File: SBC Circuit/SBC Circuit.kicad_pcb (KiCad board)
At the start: 2 copper layers, 127 x 114.3 mm, 82 parts, among them J1 USB_B, J2 Conn_01x02_Pin, J3 Conn_01x06_Pin, J4 Conn_01x06_Pin, J5 Conn_01x03_Pin, J6 Conn_01x08_Pin, J7 Conn_01x06_Pin, J8 Conn_01x02_Pin, J9 Conn_02x04_Odd_Even, Q1 AOI21357, Q2 AOI21357, SW1 RESET, U1 MC68000FN, U10 FT230XS, U11 MC34064P, U2 XC9572XL, U3 68681, U4 MCM6206CP, U5 MCM6206CP, U6 28C256, U7 28C256, U8 LM7805_TO220, U9 LD1117AV33, X1 SG-531, X2 EC11

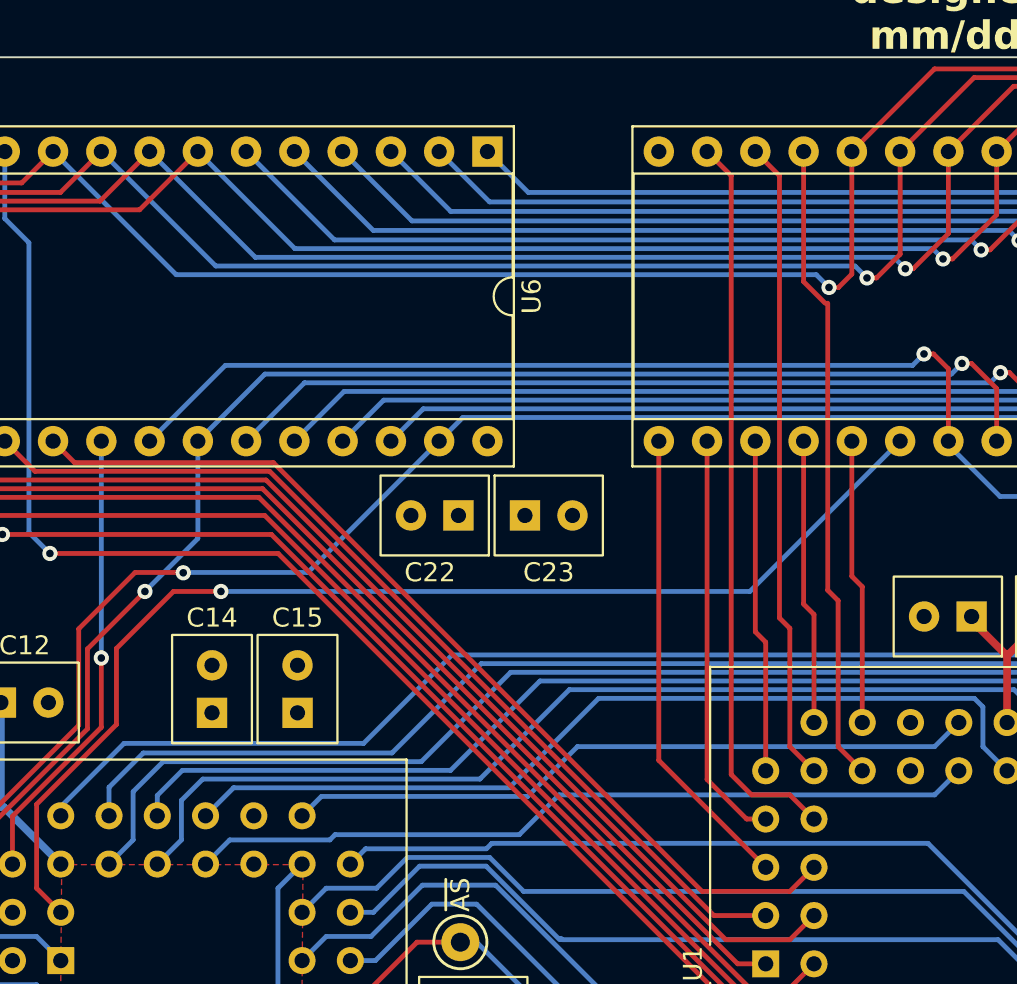
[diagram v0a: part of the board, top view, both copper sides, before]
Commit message: Wire high ROM correctly
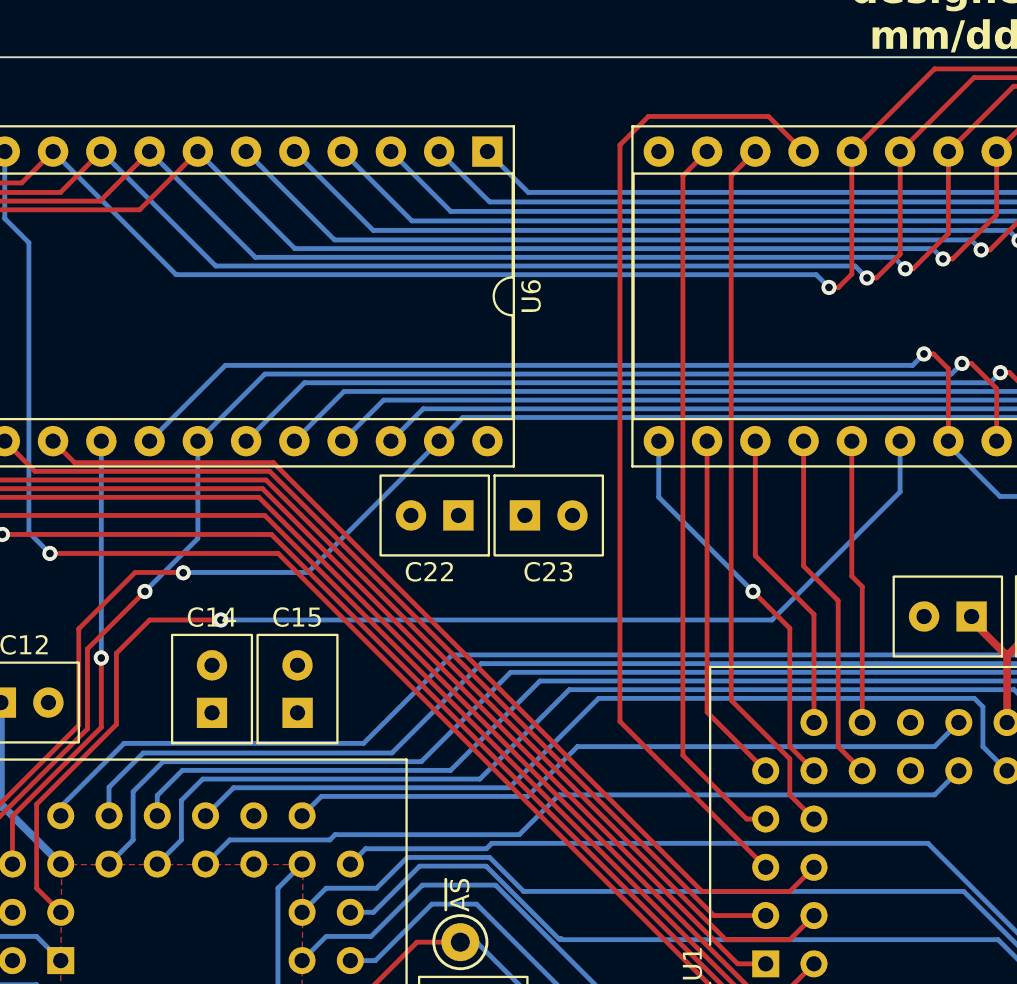
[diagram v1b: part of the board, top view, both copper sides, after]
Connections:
- U7 pad 11: data14 -> data8
- U7 pad 12: data11 -> data9
- U7 pad 13: data9 -> data10
- U7 pad 15: data8 -> data11
- U7 pad 16: data10 -> data12
- U7 pad 17: data12 -> data13
- U7 pad 18: data13 -> data14
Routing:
- net data8: track 24.8 -> 52.2 mm
- net data10: track 21.8 -> 38.0 mm
- net data14: track 33.8 -> 18.6 mm
- net data11: track 33.9 -> 20.7 mm, vias 0 -> 1
- net romh_cs: track 61.9 -> 63.3 mm
- net data9: track 38.6 -> 37.5 mm
- net data13: track 15.0 -> 16.1 mm
- net data12: track 17.8 -> 18.6 mm
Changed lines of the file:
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@@
       (net 67 "addr0") (pinfunction "A0") (pintype "input"))
     (pad "11" thru_hole oval (at 0 25.4 270) (size 1.6 1.6) (drill 0.8) (layers "*.Cu" "*.Mask")
-      (net 91 "data14") (pinfunction "D0") (pintype "tri_state"))
+      (net 97 "data8") (pinfunction "D0") (pintype "tri_state"))
     (pad "12" thru_hole oval (at 0 27.94 270) (size 1.6 1.6) (drill 0.8) (layers "*.Cu" "*.Mask")
-      (net 94 "data11") (pinfunction "D1") (pintype "tri_state"))
+      (net 96 "data9") (pinfunction "D1") (pintype "tri_state"))
     (pad "13" thru_hole oval (at 0 30.48 270) (size 1.6 1.6) (drill 0.8) (layers "*.Cu" "*.Mask")
-      (net 96 "data9") (pinfunction "D2") (pintype "tri_state"))
+      (net 95 "data10") (pinfunction "D2") (pintype "tri_state"))
     (pad "14" thru_hole oval (at 0 33.02 270) (size 1.6 1.6) (drill 0.8) (layers "*.Cu" "*.Mask")
       (net 2 "GNDREF") (pinfunction "GND") (pintype "power_in"))
     (pad "15" thru_hole oval (at 15.24 33.02 270) (size 1.6 1.6) (drill 0.8) (layers "*.Cu" "*.Mask")
-      (net 97 "data8") (pinfunction "D3") (pintype "tri_state"))
+      (net 94 "data11") (pinfunction "D3") (pintype "tri_state"))
     (pad "16" thru_hole oval (at 15.24 30.48 270) (size 1.6 1.6) (drill 0.8) (layers "*.Cu" "*.Mask")
-      (net 95 "data10") (pinfunction "D4") (pintype "tri_state"))
+      (net 93 "data12") (pinfunction "D4") (pintype "tri_state"))
     (pad "17" thru_hole oval (at 15.24 27.94 270) (size 1.6 1.6) (drill 0.8) (layers "*.Cu" "*.Mask")
-      (net 93 "data12") (pinfunction "D5") (pintype "tri_state"))
+      (net 92 "data13") (pinfunction "D5") (pintype "tri_state"))
     (pad "18" thru_hole oval (at 15.24 25.4 270) (size 1.6 1.6) (drill 0.8) (layers "*.Cu" "*.Mask")
-      (net 92 "data13") (pinfunction "D6") (pintype "tri_state"))
+      (net 91 "data14") (pinfunction "D6") (pintype "tri_state"))
     (pad "19" thru_hole oval (at 15.24 22.86 270) (size 1.6 1.6) (drill 0.8) (layers "*.Cu" "*.Mask")
       (net 90 "data15") (pinfunction "D7") (pintype "tri_state"))
@@
   (segment (start 176.33 70.935) (end 175.06 72.205) (width 0.254) (layer "B.Cu") (net 89))
   (segment (start 143.5072 74.2978) (end 143.23 74.575) (width 0.254) (layer "B.Cu") (net 89))
+  (segment (start 170.703 53.589) (end 170.703 60.703) (width 0.254) (layer "F.Cu") (net 90))
   (segment (start 171.25 61.25) (end 170.703 60.703) (width 0.254) (layer "F.Cu") (net 90))
-  (segment (start 170.703 60.703) (end 170.703 53.589) (width 0.254) (layer "F.Cu") (net 90))
   (segment (start 171.25 68.395) (end 171.25 61.25) (width 0.254) (layer "F.Cu") (net 90))
-  (segment (start 168.163 45.195659) (end 168.163 38.349) (width 0.254) (layer "F.Cu") (net 91))
   (segment (start 169.98 69.665) (end 169.98 61.98) (width 0.254) (layer "F.Cu") (net 91))
-  (segment (start 169.98 61.98) (end 169.433 61.433) (width 0.254) (layer "F.Cu") (net 91))
-  (segment (start 169.2932 46.325859) (end 168.163 45.195659) (width 0.254) (layer "F.Cu") (net 91))
+  (segment (start 168.163 60.163) (end 168.163 53.589) (width 0.254) (layer "F.Cu") (net 91))
+  (segment (start 169.98 61.98) (end 168.163 60.163) (width 0.254) (layer "F.Cu") (net 91))
   (segment (start 171.25 70.935) (end 169.98 69.665) (width 0.254) (layer "F.Cu") (net 91))
-  (segment (start 169.433 61.433) (end 169.433 46.325859) (width 0.254) (layer "F.Cu") (net 91))
+  (segment (start 165.623 59.623) (end 165.623 53.589) (width 0.254) (layer "F.Cu") (net 92))
   (segment (start 168.71 68.395) (end 168.71 62.71) (width 0.254) (layer "F.Cu") (net 92))
-  (segment (start 168.71 62.71) (end 168.163 62.163) (width 0.254) (layer "F.Cu") (net 92))
-  (segment (start 168.163 62.163) (end 168.163 53.589) (width 0.254) (layer "F.Cu") (net 92))
-  (segment (start 165.623 63.623) (end 166.17 64.17) (width 0.254) (layer "F.Cu") (net 93))
-  (segment (start 166.17 64.17) (end 166.17 70.935) (width 0.254) (layer "F.Cu") (net 93))
-  (segment (start 166.17 70.935) (end 166 70.765) (width 0.254) (layer "F.Cu") (net 93))
-  (segment (start 165.623 53.589) (end 165.623 63.623) (width 0.254) (layer "F.Cu") (net 93))
-  (segment (start 166.893 62.893) (end 166.893 39.619) (width 0.254) (layer "F.Cu") (net 94))
-  (segment (start 168.71 70.935) (end 167.44 69.665) (width 0.254) (layer "F.Cu") (net 94))
-  (segment (start 167.44 63.44) (end 166.893 62.893) (width 0.254) (layer "F.Cu") (net 94))
-  (segment (start 166.893 39.619) (end 165.623 38.349) (width 0.254) (layer "F.Cu") (net 94))
-  (segment (start 167.44 69.665) (end 167.44 63.44) (width 0.254) (layer "F.Cu") (net 94))
-  (segment (start 163.083 53.589) (end 163.083 71.393788) (width 0.254) (layer "F.Cu") (net 95))
+  (segment (start 168.71 62.71) (end 165.623 59.623) (width 0.254) (layer "F.Cu") (net 92))
+  (segment (start 166.17 70.935) (end 163.083 67.848) (width 0.254) (layer "F.Cu") (net 93))
+  (segment (start 163.083 67.848) (end 163.083 53.589) (width 0.254) (layer "F.Cu") (net 93))
+  (segment (start 167.44 69.665) (end 168.71 70.935) (width 0.254) (layer "F.Cu") (net 94))
+  (segment (start 167.44 63.44) (end 167.44 69.665) (width 0.254) (layer "F.Cu") (net 94))
+  (segment (start 165.5 61.5) (end 167.44 63.44) (width 0.254) (layer "F.Cu") (net 94))
+  (via (at 165.5 61.5) (size 0.8) (drill 0.4) (layers "F.Cu" "B.Cu") (net 94))
+  (segment (start 165.5 61.5) (end 160.543 56.543) (width 0.254) (layer "B.Cu") (net 94))
+  (segment (start 160.543 56.543) (end 160.543 53.589) (width 0.254) (layer "B.Cu") (net 94))
+  (segment (start 163.083 38.349) (end 161.813 39.619) (width 0.254) (layer "F.Cu") (net 95))
   (segment (start 165.164212 73.475) (end 166.17 73.475) (width 0.254) (layer "F.Cu") (net 95))
-  (segment (start 163.083 71.393788) (end 165.164212 73.475) (width 0.254) (layer "F.Cu") (net 95))
-  (segment (start 164.353 39.619) (end 164.353 71.135) (width 0.254) (layer "F.Cu") (net 96))
-  (segment (start 167.44 72.205) (end 168.71 73.475) (width 0.254) (layer "F.Cu") (net 96))
-  (segment (start 165.423 72.205) (end 167.44 72.205) (width 0.254) (layer "F.Cu") (net 96))
-  (segment (start 164.353 71.135) (end 165.423 72.205) (width 0.254) (layer "F.Cu") (net 96))
-  (segment (start 163.083 38.349) (end 164.353 39.619) (width 0.254) (layer "F.Cu") (net 96))
-  (segment (start 166.17 76.015) (end 160.543 70.388) (width 0.254) (layer "F.Cu") (net 97))
-  (segment (start 160.543 70.388) (end 160.543 53.589) (width 0.254) (layer "F.Cu") (net 97))
+  (segment (start 161.813 39.619) (end 161.813 70.123788) (width 0.254) (layer "F.Cu") (net 95))
+  (segment (start 161.813 70.123788) (end 165.164212 73.475) (width 0.254) (layer "F.Cu") (net 95))
+  (segment (start 168.71 73.475) (end 167.44 72.205) (width 0.254) (layer "F.Cu") (net 96))
+  (segment (start 164.353 67.224578) (end 164.353 39.619) (width 0.254) (layer "F.Cu") (net 96))
+  (segment (start 167.44 72.205) (end 167.44 70.311578) (width 0.254) (layer "F.Cu") (net 96))
+  (segment (start 167.44 70.311578) (end 164.353 67.224578) (width 0.254) (layer "F.Cu") (net 96))
+  (segment (start 164.353 39.619) (end 165.623 38.349) (width 0.254) (layer "F.Cu") (net 96))
+  (segment (start 160 36.5) (end 166.314 36.5) (width 0.254) (layer "F.Cu") (net 97))
+  (segment (start 166.17 76.015) (end 158.5 68.345) (width 0.254) (layer "F.Cu") (net 97))
+  (segment (start 158.5 68.345) (end 158.5 38) (width 0.254) (layer "F.Cu") (net 97))
+  (segment (start 158.5 38) (end 160 36.5) (width 0.254) (layer "F.Cu") (net 97))
+  (segment (start 166.314 36.5) (end 168.163 38.349) (width 0.254) (layer "F.Cu") (net 97))
   (segment (start 111.87 88.295) (end 132.42 108.845) (width 0.254) (layer "F.Cu") (net 98))
   (segment (start 129.7952 54.7192) (end 128.665 53.589) (width 0.254) (layer "F.Cu") (net 98))
@@
   (via (at 131.205 65) (size 0.8) (drill 0.4) (layers "F.Cu" "B.Cu") (net 107))
   (segment (start 131.205 53.589) (end 131.205 65) (width 0.254) (layer "B.Cu") (net 107))
-  (segment (start 137.5 61.5) (end 135 61.5) (width 0.254) (layer "F.Cu") (net 108))
-  (segment (start 132 64.5) (end 132 68.5) (width 0.254) (layer "F.Cu") (net 108))
-  (segment (start 135 61.5) (end 132 64.5) (width 0.254) (layer "F.Cu") (net 108))
   (segment (start 127.8 72.7) (end 127.8 77.115) (width 0.254) (layer "F.Cu") (net 108))
-  (segment (start 127.8 77.115) (end 129.07 78.385) (width 0.254) (layer "F.Cu") (net 108))
   (segment (start 132 68.5) (end 127.8 72.7) (width 0.254) (layer "F.Cu") (net 108))
-  (via (at 137.5 61.5) (size 0.8) (drill 0.4) (layers "F.Cu" "B.Cu") (net 108))
-  (segment (start 165.332 61.5) (end 173.243 53.589) (width 0.254) (layer "B.Cu") (net 108))
-  (segment (start 137.5 61.5) (end 165.332 61.5) (width 0.254) (layer "B.Cu") (net 108))
+  (segment (start 127.8 77.115) (end 129.07 78.385) (width 0.254) (layer "F.Cu") (net 108))
+  (segment (start 133.75 63) (end 132 64.75) (width 0.254) (layer "F.Cu") (net 108))
+  (segment (start 132 64.75) (end 132 68.5) (width 0.254) (layer "F.Cu") (net 108))
+  (segment (start 137.5 63) (end 133.75 63) (width 0.254) (layer "F.Cu") (net 108))
+  (via (at 137.5 63) (size 0.8) (drill 0.4) (layers "F.Cu" "B.Cu") (net 108))
+  (segment (start 173.243 56.257) (end 173.243 53.589) (width 0.254) (layer "B.Cu") (net 108))
+  (segment (start 166.5 63) (end 173.243 56.257) (width 0.254) (layer "B.Cu") (net 108))
+  (segment (start 137.5 63) (end 166.5 63) (width 0.254) (layer "B.Cu") (net 108))
   (segment (start 147.82 79.955) (end 144.31 83.465) (width 0.254) (layer "F.Cu") (net 109))
   (segment (start 150.1 79.955) (end 147.82 79.955) (width 0.254) (layer "F.Cu") (net 109))

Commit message: Add graphic
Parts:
- added G***: LOGO, LOGO, F.Cu at (36.7, 137.1)
- added G***: LOGO, LOGO, F.Cu at (44.0, 66.8)
- added G***: LOGO, LOGO, F.Cu at (43.0, 96.5)
- added G***: LOGO, LOGO, F.Cu at (108.8, 78.5)
- added G***: LOGO, LOGO, F.Cu at (114.0, 79.5)
- added G***: LOGO, LOGO, F.Cu at (31.0, 127.0)
- added G***: LOGO, LOGO, F.Cu at (32.0, 96.0)
- added G***: LOGO, LOGO, F.Cu at (48.0, 131.0)
- moved G*** 136.5 mm to (20.5, 181.5)
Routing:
- net +3.3V: track 159.6 -> 181.9 mm
- net /Power+IO/serial_3.3: track 30.8 -> 26.6 mm, vias 0 -> 1

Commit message: Create 11x17
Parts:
- moved G*** 42.3 mm to (34.2, 179.3)
- moved G*** 42.3 mm to (41.5, 109.0)
- moved G*** 42.3 mm to (40.5, 138.8)
- moved G*** 42.3 mm to (28.5, 169.2)
- moved G*** 42.3 mm to (29.5, 138.2)
- moved G*** 42.3 mm to (45.5, 173.2)
- moved C20 37.4 mm to (198.5, 123.5), turned to 90 degrees
- moved C18 35.5 mm to (196.4, 143.4), turned to 0 degrees
- moved C21 35.4 mm to (194.5, 127.5), turned to 180 degrees
- moved C19 33.0 mm to (192.9, 143.4), turned to 180 degrees
- moved U4 31.3 mm to (194.6, 131.6), turned to -90 degrees
- moved U5 30.3 mm to (194.6, 115.9), turned to -90 degrees
- moved R4 2.63 mm to (181.5, 105.7), turned to 90 degrees
- moved SW1 1.77 mm to (192.0, 109.0)
- moved U11 1.42 mm to (187.5, 103.7), turned to -90 degrees
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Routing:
- net raml_cs: track 76.0 -> 27.3 mm
- net ramh_cs: track 66.7 -> 23.4 mm
- net +3.3V: track 181.9 -> 171.8 mm
- net /rw: track 18.4 -> 25.5 mm
- net /uds: track 17.4 -> 24.1 mm
- net /lds: track 19.4 -> 25.9 mm
- net hlt_rst: track 68.5 -> 62.0 mm
- net +5V: track 270.4 -> 275.7 mm
- net /n6: track 14.5 -> 12.3 mm
- net data0: track 137.5 -> 138.5 mm
- net data1: track 150.9 -> 150.2 mm
- net /fc1: track 53.5 -> 54.1 mm

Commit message: Commit before design change 2
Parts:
- moved C8 0.82 mm to (180.9, 62.0), turned to 90 degrees
- moved C9 0.82 mm to (177.0, 62.0), turned to 90 degrees
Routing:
- net /fc2: track 55.3 -> 12.9 mm
- net /ipl1: track 53.7 -> 11.8 mm
- net /fc0: track 54.3 -> 17.3 mm
- net /ipl0: track 54.6 -> 18.0 mm
- net /fc1: track 54.1 -> 25.7 mm
- net addr17: track 61.7 -> 46.2 mm
- net addr15: track 65.5 -> 50.5 mm
- net addr16: track 58.7 -> 45.0 mm
- net addr19: track 55.3 -> 42.6 mm
- net (no net): track 0.00 -> 11.5 mm
- net addr18: track 52.3 -> 41.3 mm
- net /dtack: track 26.3 -> 35.8 mm
- net +5V: track 275.7 -> 284.8 mm
- net data3: track 146.4 -> 137.9 mm
- net addr20: track 47.5 -> 39.6 mm
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
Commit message: Wire phase done
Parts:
- added TP7: ~{BERR}, TestPoint:TestPoint_Keystone_5000-5004_Miniature, F.Cu at (146.5, 91.5)
- TP2: value 3V TEST -> 3.3V TEST
- moved G*** 45.9 mm to (63.0, 75.0)
- moved G*** 45.6 mm to (68.5, 76.0)
- moved TP6 16.0 mm to (144.5, 78.0)
- moved TP5 9.73 mm to (144.5, 72.0)
- moved C18 8.27 mm to (198.5, 135.4), turned to 90 degrees
- moved C19 7.18 mm to (198.5, 138.9), turned to -90 degrees
- moved C10 5.32 mm to (144.5, 82.3)
- moved C11 5.32 mm to (144.5, 86.8)
- moved C14 5.32 mm to (132.0, 66.3)
- moved C15 5.32 mm to (136.5, 66.3)
- moved C13 5.32 mm to (115.7, 71.2)
- moved U2 5.32 mm to (124.0, 79.3)
- moved C12 5.14 mm to (120.8, 66.5), turned to 90 degrees
- moved J3 5.09 mm to (130.3, 97.5)
- moved C21 4.14 mm to (198.5, 126.4), turned to -90 degrees
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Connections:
- U2 pad 12: /berr -> /fc1
- U2 pad 13: /ipl2 -> /ipl0
- U2 pad 14: /dtack -> /fc2
- U2 pad 18: /lds -> /fc0
- U2 pad 19: /rw -> /ipl1
- U2 pad 20: /uds -> /berr
- U2 pad 22: /as -> /ipl2
- U2 pad 24: /ipl1 -> /dtack
- U2 pad 25: /fc2 -> /rw
- U2 pad 26: /ipl0 -> /lds
- U2 pad 27: /fc0 -> /uds
- U2 pad 28: /fc1 -> /as
- U4 pad 1: addr14 -> addr5
- U4 pad 10: addr0 -> addr14
- U4 pad 15: data3 -> data7
- U4 pad 16: data4 -> data6
- U4 pad 18: data6 -> data4
- U4 pad 19: data7 -> data3
- U4 pad 2: addr12 -> addr8
- U4 pad 21: addr10 -> addr9
- U4 pad 23: addr11 -> addr10
- U4 pad 24: addr9 -> addr11
- U4 pad 25: addr8 -> addr13
- U4 pad 26: addr13 -> addr12
- U4 pad 5: addr5 -> addr3
- U4 pad 7: addr3 -> addr1
- U4 pad 9: addr1 -> addr0
- U5 pad 1: addr14 -> addr5
- U5 pad 10: addr0 -> addr14
- U5 pad 11: data8 -> data15
- U5 pad 12: data9 -> data14
- U5 pad 13: data10 -> data8
- U5 pad 15: data11 -> data13
- U5 pad 17: data13 -> data11
- U5 pad 18: data14 -> data10
- U5 pad 19: data15 -> data9
- U5 pad 2: addr12 -> addr8
- U5 pad 21: addr10 -> addr9
- U5 pad 23: addr11 -> addr10
- U5 pad 24: addr9 -> addr11
- U5 pad 25: addr8 -> addr13
- U5 pad 26: addr13 -> addr12
- U5 pad 5: addr5 -> addr3
- U5 pad 7: addr3 -> addr1
- U5 pad 9: addr1 -> addr0
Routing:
- net addr13: track 63.4 -> 157.4 mm, vias 1 -> 2
- net addr14: track 71.9 -> 164.2 mm
- net addr12: track 73.6 -> 165.0 mm, vias 1 -> 2
- net addr9: track 70.2 -> 161.0 mm, vias 1 -> 2
- net addr10: track 77.9 -> 168.1 mm, vias 1 -> 2
- net addr11: track 69.1 -> 156.5 mm, vias 1 -> 2
- net data5: track 130.2 -> 208.1 mm, vias 0 -> 1
- net data7: track 123.4 -> 201.2 mm, vias 0 -> 1
- net data3: track 137.9 -> 215.3 mm, vias 0 -> 1
- net we: track 93.9 -> 169.1 mm
- net data4: track 114.8 -> 189.9 mm, vias 0 -> 1
- net data6: track 108.0 -> 182.7 mm, vias 0 -> 1
- net data9: track 37.5 -> 112.2 mm
- net data13: track 16.1 -> 88.9 mm
- net data10: track 37.6 -> 109.5 mm
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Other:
- board text added: "designed by Richard Homan Spring 2024 — revision 0.0"
- board text removed: "designed by Richard Homan mm/dd/2024 — revision 0.0"
